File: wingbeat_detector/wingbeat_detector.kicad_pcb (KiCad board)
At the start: 2 copper layers, 36 x 18 mm, 24 parts, among them J1 USB_C_10137062-00021LF, J2 CONN_UMC_JACK_SMD, J3 CONN_UMC_JACK_SMD, Q1 MOSFET-N-CH, U1 LED_DRV_50mA, U2 MAX865EUA+, U3 UAF42_SMA, U4 UAF42_SMA, U5 OPA381

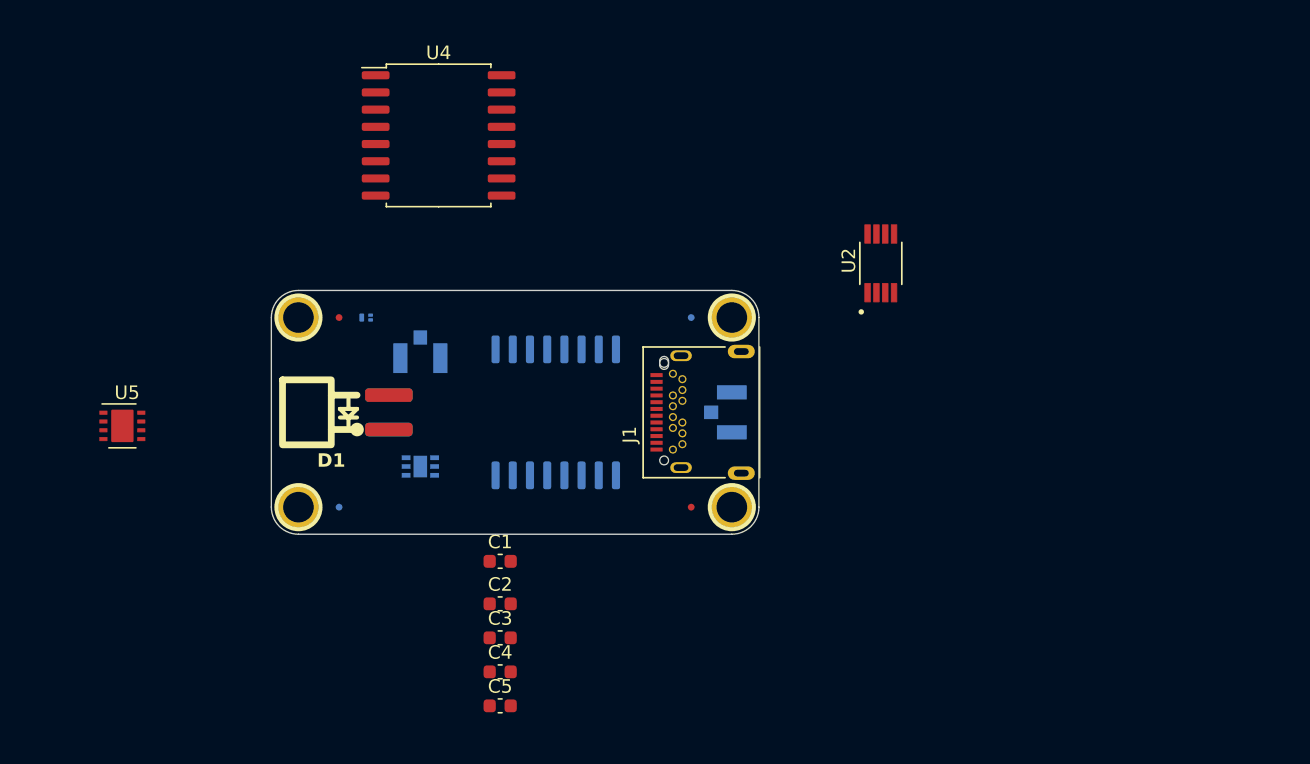
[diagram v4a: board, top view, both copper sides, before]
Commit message: Remove connectors schematic sheet
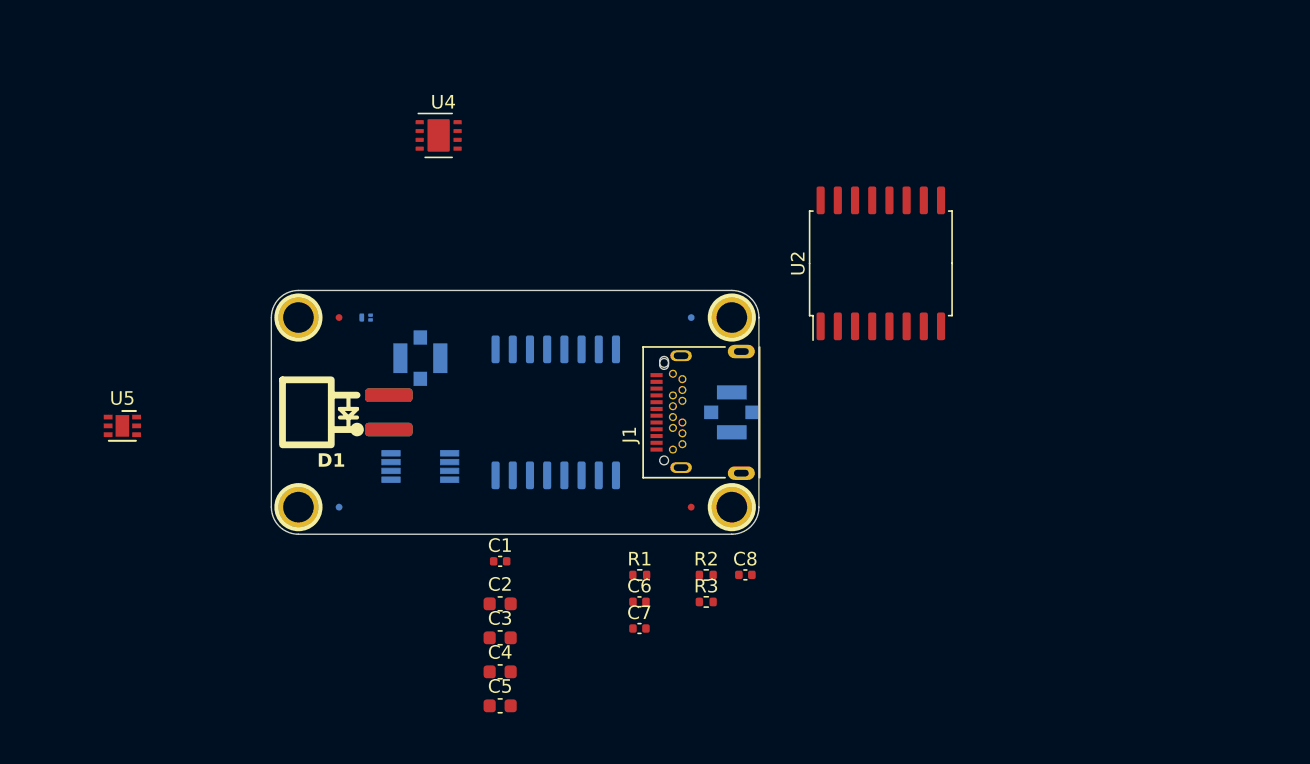
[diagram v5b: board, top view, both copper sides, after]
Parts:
- added C6: 1uF, Janelia:C_0402_1005Metric, F.Cu at (159.2, 114.0)
- added C7: 2pF, Janelia:C_0402_1005Metric, F.Cu at (159.2, 116.0)
- added C8: 1uF, Janelia:C_0402_1005Metric, F.Cu at (167.0, 112.0)
- added R1: 49.9k, Janelia:R_0402_1005Metric, F.Cu at (159.2, 112.0)
- added R2: 49.9k, Janelia:R_0402_1005Metric, F.Cu at (164.1, 112.0)
- added R3: 49.9k, Janelia:R_0402_1005Metric, F.Cu at (164.1, 114.0)
- C1: value 4.7uF -> 1uF; footprint Janelia:C_0603_1608Metric -> Janelia:C_0402_1005Metric
- H1, H2, H3, H4: value MOUNTING_HOLE_2 -> VAL**
- U1: value LED_DRV_50mA -> MAX865EUA+; footprint Janelia:DFN-6-1EP_2x2mm_P0.65mm_EP1x1.6mm -> Janelia:SOP65P490X110-8N
- U2: value MAX865EUA+ -> UAF42_SMA; footprint Janelia:SOP65P490X110-8N -> Janelia:SOIC-16W_7.5x10.3mm_P1.27mm
- U4: value UAF42_SMA -> OPA381; footprint Janelia:SOIC-16W_7.5x10.3mm_P1.27mm -> Janelia:VSON-8-1EP_3x3mm_P0.65mm_EP1.65x2.4mm
- U5: value OPA381 -> LED_DRV_50mA; footprint Janelia:VSON-8-1EP_3x3mm_P0.65mm_EP1.65x2.4mm -> Janelia:DFN-6-1EP_2x2mm_P0.65mm_EP1x1.6mm
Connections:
- net /LED_ENABLE renamed /led/LED_ENABLE
- net /PHOTODIODE_FILTERED renamed /filter/PHOTODIODE_FILTERED
- D1 pad 1: unconnected-(D1-K-Pad1) -> Net-(D1-K)
- D1 pad 2: unconnected-(D1-A-Pad2) -> /GND
- J2 pad 2: /GND -> /filter/GND
- U1 pad 1: Net-(D2-A) -> /power/C1-
- U1 pad 2: (no net) -> /power/C2+
- U1 pad 3: Net-(D2-K) -> /power/C2-
- U1 pad 4: /led/VB -> /V10-
- U1 pad 5: (no net) -> /GND
- U1 pad 7: /GND -> /V10+
- U2 pad 1: /power/C1- -> unconnected-(U2-LPVo-Pad1)
- U2 pad 2: /power/C2+ -> unconnected-(U2-NC1-Pad2)
- U2 pad 3: /power/C2- -> unconnected-(U2-Vin3-Pad3)
- U2 pad 4: /V10- -> unconnected-(U2-Vin2-Pad4)
- U2 pad 5: /GND -> unconnected-(U2-AAin+-Pad5)
- U2 pad 6: /V5+ -> unconnected-(U2-AAin--Pad6)
- U2 pad 7: /V10+ -> unconnected-(U2-AAVo-Pad7)
- U2 pad 8: /power/C1+ -> unconnected-(U2-BPVo-Pad8)
- U4 pad 1: unconnected-(U4-LPVo-Pad1) -> (no net)
- U4 pad 2: unconnected-(U4-NC1-Pad2) -> Net-(D1-K)
- U4 pad 3: unconnected-(U4-Vin3-Pad3) -> /GND
- U4 pad 4: unconnected-(U4-Vin2-Pad4) -> /GND
- U4 pad 5: unconnected-(U4-AAin+-Pad5) -> (no net)
- U4 pad 6: unconnected-(U4-AAin--Pad6) -> /PHOTODIODE_RAW
- U4 pad 7: unconnected-(U4-AAVo-Pad7) -> /V5+
- U4 pad 8: unconnected-(U4-BPVo-Pad8) -> (no net)
- U4 pad 9: unconnected-(U4-Fadj1-Pad9) -> /GND
- U5 pad 1: (no net) -> Net-(D2-A)
- U5 pad 2: unconnected-(U5---Pad2) -> (no net)
- U5 pad 3: unconnected-(U5-+-Pad3) -> Net-(D2-K)
- U5 pad 4: unconnected-(U5-V--Pad4) -> /led/VB
- U5 pad 6: unconnected-(U5-Pad6) -> /V5+
- U5 pad 7: unconnected-(U5-V+-Pad7) -> /GND

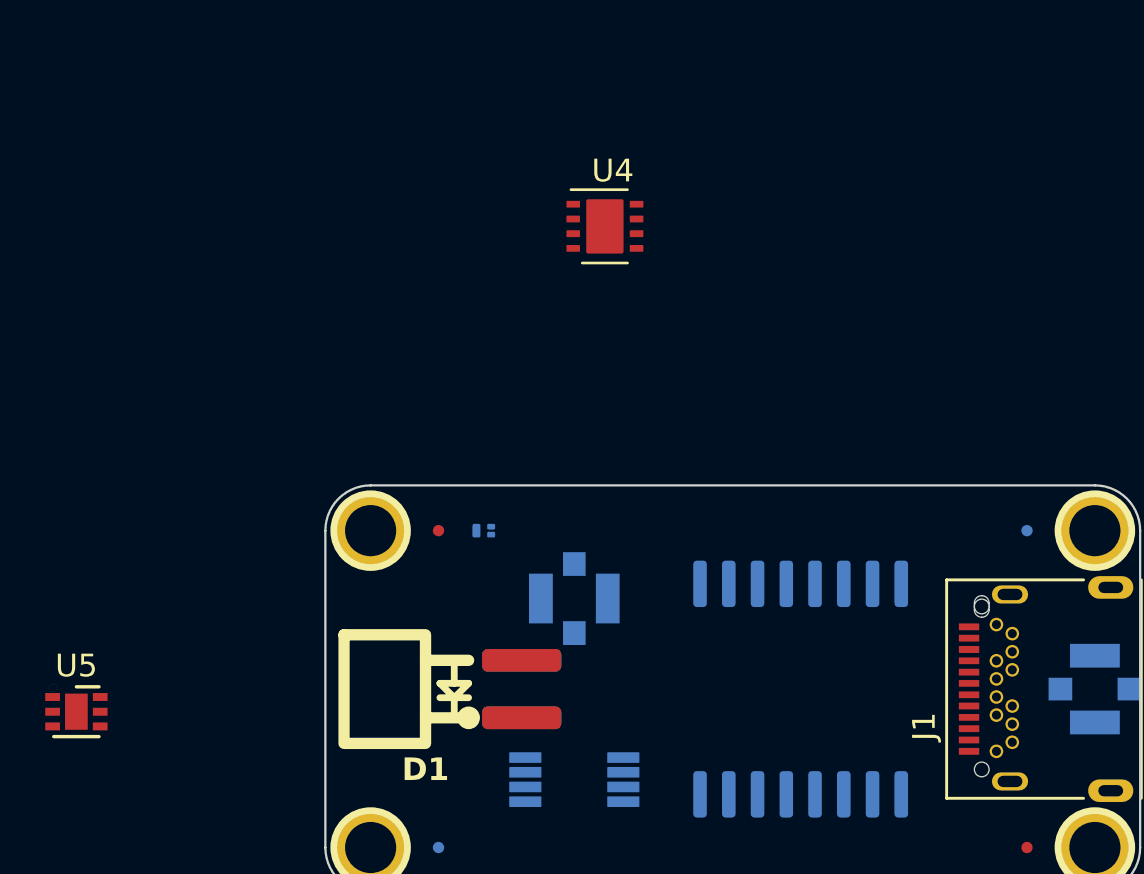
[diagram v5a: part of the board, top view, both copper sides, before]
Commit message: Add buffered output
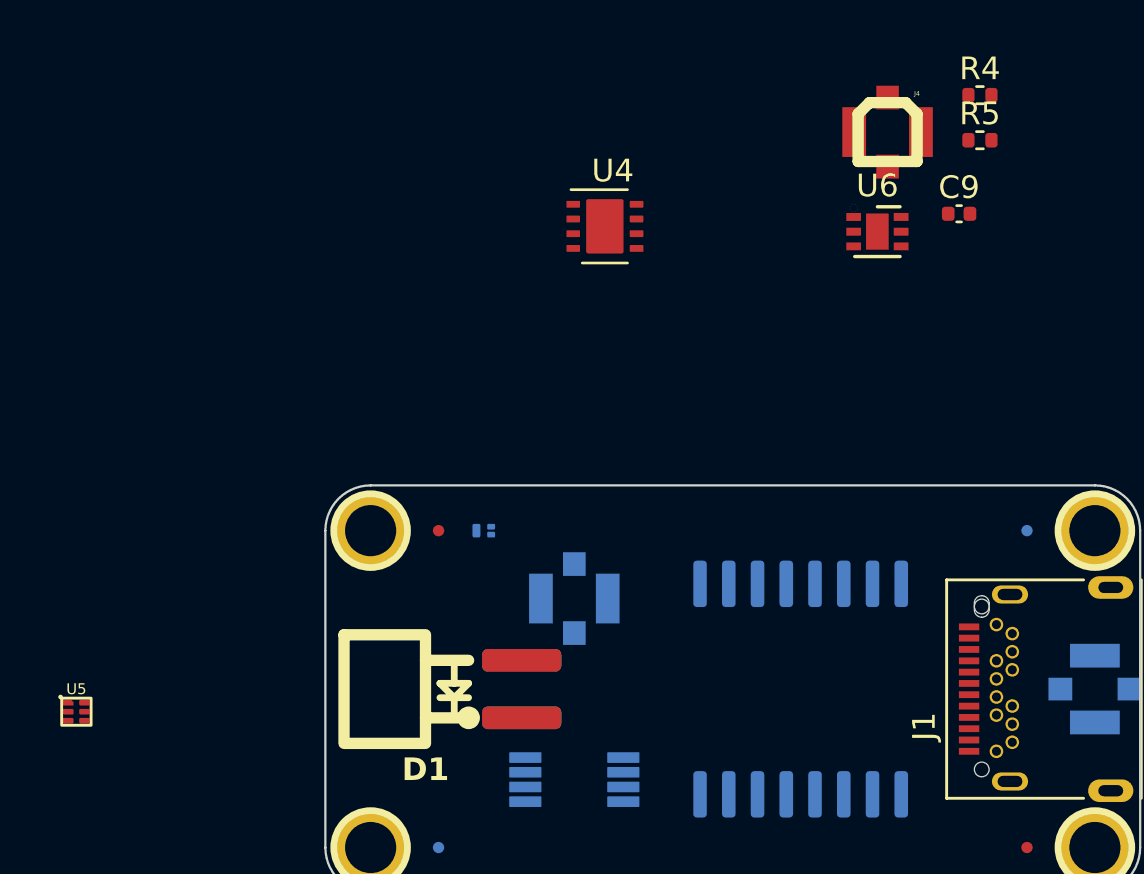
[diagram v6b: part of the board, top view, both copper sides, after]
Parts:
- added C9: 1uF, Janelia:C_0402_1005Metric, F.Cu at (160.0, 79.0)
- added J4: CONN_UMC_JACK_SMD, Janelia:UMC_AMPHENOL_A-1JB, F.Cu at (156.8, 75.4)
- added R4: 23.2k, Janelia:R_0402_1005Metric, F.Cu at (160.9, 73.8)
- added R5: 49.9k, Janelia:R_0402_1005Metric, F.Cu at (160.9, 75.8)
- added U6: LED_DRV_50mA, Janelia:DFN-6-1EP_2x2mm_P0.65mm_EP1x1.6mm, F.Cu at (156.4, 79.8)
- H1, H2, H3, H4: value VAL** -> MOUNTING_HOLE_2
- R2: value 49.9k -> 23.2k
- U5: value LED_DRV_50mA -> TSV630IQ1T; footprint Janelia:DFN-6-1EP_2x2mm_P0.65mm_EP1x1.6mm -> Janelia:PSON40P120X130X50-6N
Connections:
- H1 pad 1: unconnected-(H1-Pad1) -> /GND
- H2 pad 1: unconnected-(H2-Pad1) -> /GND
- H3 pad 1: unconnected-(H3-Pad1) -> /GND
- H4 pad 1: unconnected-(H4-Pad1) -> /GND
- J3 pad 1: /led/LED_ENABLE -> /photodiode/PHOTODIODE_BUFFERED
- R2 pad 1: /V5+ -> Net-(U5--)
- R2 pad 2: /led/LED_ENABLE -> /photodiode/PHOTODIODE_BUFFERED
- R3 pad 1: /led/LED_ENABLE -> /photodiode/PHOTODIODE_BUFFERED
- U5 pad 1: Net-(D2-A) -> Net-(U5--)
- U5 pad 2: (no net) -> /GND
- U5 pad 3: Net-(D2-K) -> Net-(U5--)
- U5 pad 4: /led/VB -> /PHOTODIODE_RAW
- U5 pad 5: (no net) -> /V5+

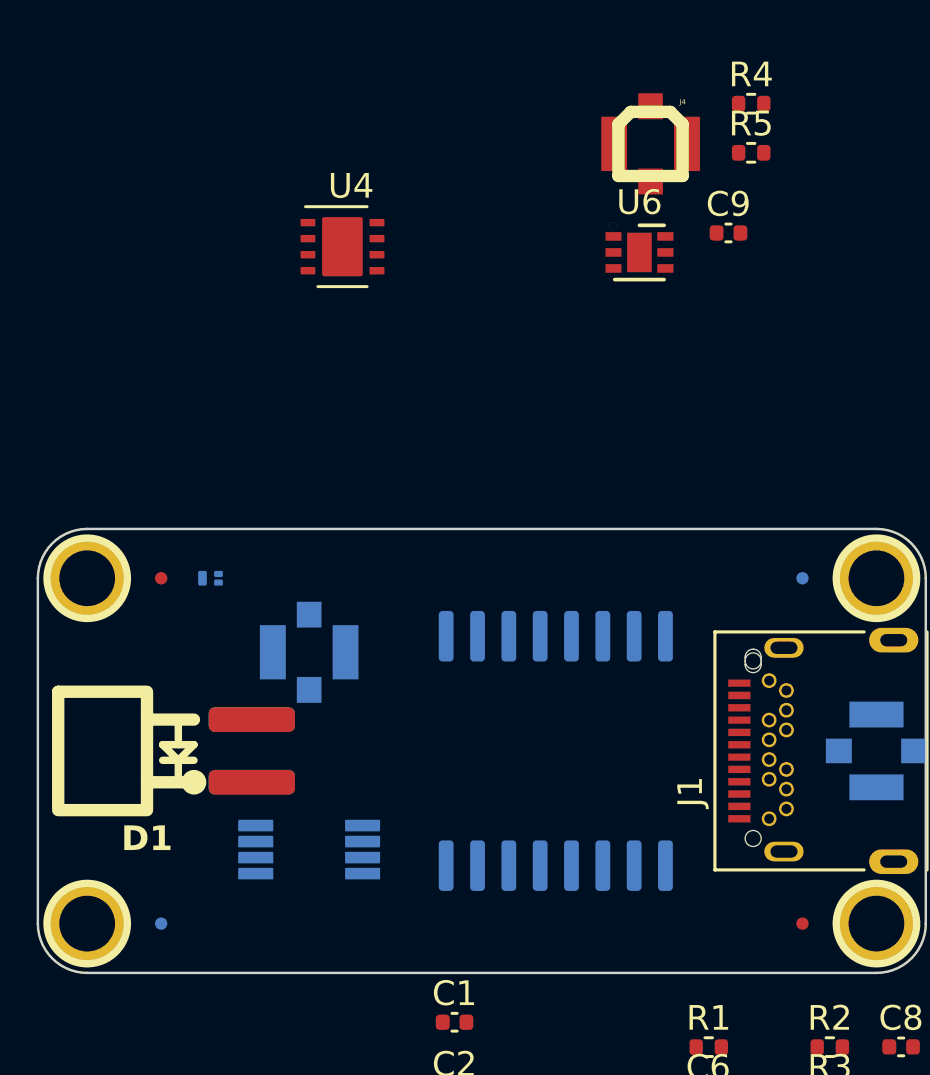
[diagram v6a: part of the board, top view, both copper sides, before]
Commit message: Initial schematic layout
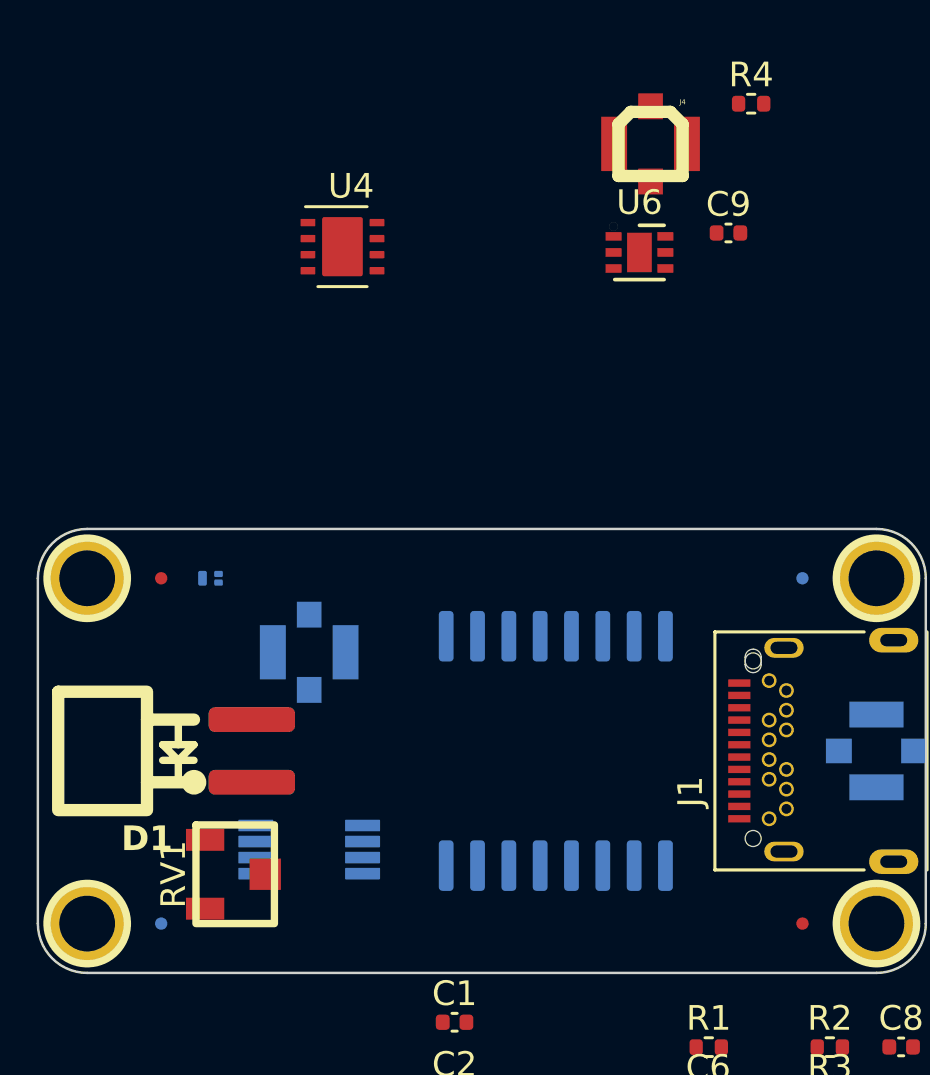
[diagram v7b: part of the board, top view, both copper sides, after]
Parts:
- removed R5: 49.9k, Janelia:R_0402_1005Metric
- added RV1: 500k, Janelia:Potentiometer_Bourns_3223W_Vertical, F.Cu at (140.0, 105.0)
- R1, R3: value 49.9k -> 23.2k
- R2, R4: value 23.2k -> 49.9k
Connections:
- R1 pad 1: Net-(D1-K) -> Net-(U5--)
- R1 pad 2: /PHOTODIODE_RAW -> /photodiode/PHOTODIODE_BUFFERED
- R2 pad 1: Net-(U5--) -> /photodiode/PHOTODIODE_BUFFERED
- R2 pad 2: /photodiode/PHOTODIODE_BUFFERED -> /GND
- R3 pad 1: /photodiode/PHOTODIODE_BUFFERED -> /V5+
- R3 pad 2: /GND -> /led/LED_ENABLE
- R4 pad 1: /V5+ -> /led/LED_ENABLE
- R4 pad 2: /led/LED_ENABLE -> /GND

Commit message: Double check schematic
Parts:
- added C10: 0.1uF, Janelia:C_0402_1005Metric, F.Cu at (179.8, 104.5)
- added C11: 2pF, Janelia:C_0402_1005Metric, F.Cu at (179.8, 106.5)
- added C12: 0.1uF, Janelia:C_0402_1005Metric, F.Cu at (179.8, 108.5)
- added C13: 0.1uF, Janelia:C_0402_1005Metric, F.Cu at (192.5, 112.5)
- added R10: 49.9k, Janelia:R_0402_1005Metric, F.Cu at (182.7, 109.9)
- added R11: 49.9k, Janelia:R_0402_1005Metric, F.Cu at (182.7, 111.9)
- added R12: 49.9k, Janelia:R_0402_1005Metric, F.Cu at (189.6, 112.5)
- added R13: 23.2k, Janelia:R_0402_1005Metric, F.Cu at (189.6, 114.5)
- added R14: 49.9k, Janelia:R_0402_1005Metric, F.Cu at (176.5, 121.5)
- added R15: 23.2k, Janelia:R_0402_1005Metric, F.Cu at (171.6, 121.5)
- added R16: 49.9k, Janelia:R_0402_1005Metric, F.Cu at (171.6, 123.5)
- added R5: 3.65M, Janelia:R_0603_1608Metric, F.Cu at (193.1, 104.8)
- added R6: 49.9k, Janelia:R_0402_1005Metric, F.Cu at (189.6, 104.5)
- added R7: 3.65M, Janelia:R_0603_1608Metric, F.Cu at (193.1, 107.3)
- added R8: 49.9k, Janelia:R_0402_1005Metric, F.Cu at (189.6, 106.5)
- added R9: 249, Janelia:R_0402_1005Metric, F.Cu at (189.6, 108.5)
- added RV2: 500k, Janelia:Potentiometer_Bourns_3223W_Vertical, F.Cu at (183.8, 106.2)
- C1: value 1uF -> 4.7uF; footprint Janelia:C_0402_1005Metric -> Janelia:C_0603_1608Metric
- C6, C8, C9: value 1uF -> 0.1uF
- C7: value 2pF -> 0.1uF
- J3, U1, U3: moved to F.Cu
- R1, R3: value 23.2k -> 49.9k
- R2, R4: value 49.9k -> 68.1k
- moved U3 47.3 mm to (199.5, 91.5)
- moved RV1 24.2 mm to (117.5, 114.0)
- moved J3 21.2 mm to (133.5, 77.0), turned to 0 degrees
- moved Q1 20.2 mm to (124.5, 79.0)
- moved U1 13.2 mm to (136.5, 115.5), turned to 0 degrees
- moved FID1 5.00 mm to (133.0, 96.0)
- moved FID4 5.00 mm to (133.0, 104.0)
- moved FID2 1.12 mm to (163.5, 92.0)
- moved FID3 1.12 mm to (163.5, 108.0)
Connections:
- C6 pad 1: /V5+ -> /V10+
- C7 pad 1: Net-(D1-K) -> /V10+
- C7 pad 2: /PHOTODIODE_RAW -> /GND
- C8 pad 1: /V5+ -> /GND
- C8 pad 2: /GND -> /V10-
- C9 pad 1: /V5+ -> /GND
- C9 pad 2: /GND -> /V10-
- J2 pad 1: /filter/PHOTODIODE_FILTERED -> /filter/BANDPASS_BUFFERED
- J2 pad 2: /filter/GND -> /GND
- R1 pad 1: Net-(U5--) -> /PHOTODIODE_RAW
- R1 pad 2: /photodiode/PHOTODIODE_BUFFERED -> Net-(U2-Vin1)
- R2 pad 1: /photodiode/PHOTODIODE_BUFFERED -> Net-(U2-Vin2)
- R3 pad 1: /V5+ -> /filter/HIGHPASS_AMPLIFIED
- R3 pad 2: /led/LED_ENABLE -> Net-(U3-Vin1)
- R4 pad 1: /led/LED_ENABLE -> Net-(U3-Vin2)
- RV1 pad 1: Net-(D1-K) -> Net-(U2-AAin-)
- RV1 pad 2: /PHOTODIODE_RAW -> /filter/HIGHPASS_AMPLIFIED
- U2 pad 10: unconnected-(U2-V--Pad10) -> /V10-
- U2 pad 11: unconnected-(U2-V+-Pad11) -> /V10+
- U2 pad 12: unconnected-(U2-GND-Pad12) -> /GND
- U2 pad 13: unconnected-(U2-Vin1-Pad13) -> Net-(U2-Vin1)
- U2 pad 14: unconnected-(U2-HPVo-Pad14) -> /filter/HIGHPASS
- U2 pad 15: unconnected-(U2-NC2-Pad15) -> /GND
- U2 pad 16: unconnected-(U2-Fadj2-Pad16) -> Net-(U2-Fadj2)
- U2 pad 2: unconnected-(U2-NC1-Pad2) -> /GND
- U2 pad 4: unconnected-(U2-Vin2-Pad4) -> Net-(U2-Vin2)
- U2 pad 5: unconnected-(U2-AAin+-Pad5) -> /filter/HIGHPASS
- U2 pad 6: unconnected-(U2-AAin--Pad6) -> Net-(U2-AAin-)
- U2 pad 7: unconnected-(U2-AAVo-Pad7) -> /filter/HIGHPASS_AMPLIFIED
- U2 pad 8: unconnected-(U2-BPVo-Pad8) -> Net-(U2-BPVo)
- U2 pad 9: unconnected-(U2-Fadj1-Pad9) -> Net-(U2-Fadj1)
- U3 pad 1: unconnected-(U3-LPVo-Pad1) -> /filter/LOWPASS
- U3 pad 10: unconnected-(U3-V--Pad10) -> /V10-
- U3 pad 11: unconnected-(U3-V+-Pad11) -> /V10+
- U3 pad 12: unconnected-(U3-GND-Pad12) -> /GND
- U3 pad 13: unconnected-(U3-Vin1-Pad13) -> Net-(U3-Vin1)
- U3 pad 14: unconnected-(U3-HPVo-Pad14) -> Net-(U3-HPVo)
- U3 pad 15: unconnected-(U3-NC2-Pad15) -> /GND
- U3 pad 16: unconnected-(U3-Fadj2-Pad16) -> Net-(U3-Fadj2)
- U3 pad 2: unconnected-(U3-NC1-Pad2) -> /GND
- U3 pad 4: unconnected-(U3-Vin2-Pad4) -> Net-(U3-Vin2)
- U3 pad 5: unconnected-(U3-AAin+-Pad5) -> /filter/LOWPASS
- U3 pad 6: unconnected-(U3-AAin--Pad6) -> /filter/BANDPASS_BUFFERED
- U3 pad 7: unconnected-(U3-AAVo-Pad7) -> /filter/BANDPASS_BUFFERED
- U3 pad 8: unconnected-(U3-BPVo-Pad8) -> Net-(U3-BPVo)
- U3 pad 9: unconnected-(U3-Fadj1-Pad9) -> Net-(U3-Fadj1)
